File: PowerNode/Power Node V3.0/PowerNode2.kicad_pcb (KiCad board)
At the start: 2 copper layers, 78.4 x 64.8 mm, 60 parts, among them IC1 CD4511B, IC4 ACS712xLCTR-30A, IC5 74HC595N, IC7 CD4511B

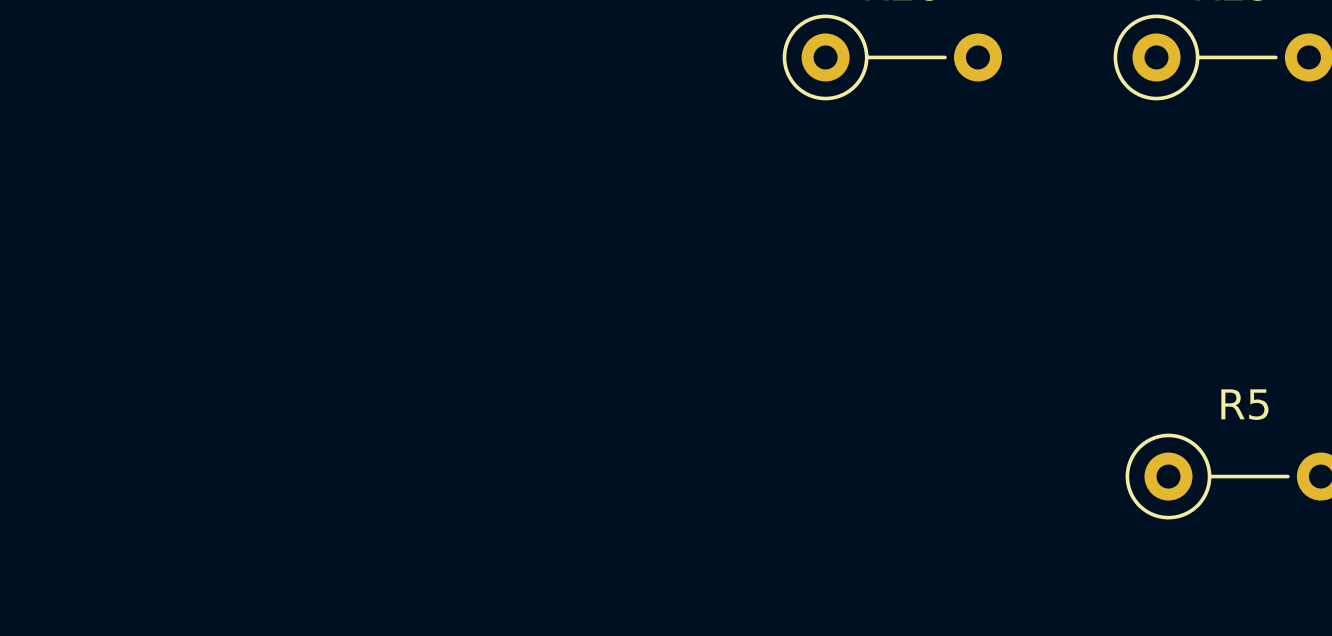
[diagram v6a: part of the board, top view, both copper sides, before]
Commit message: PN3: added logic schematic (oops) and protective diode/capacitors for ATTiny inputs
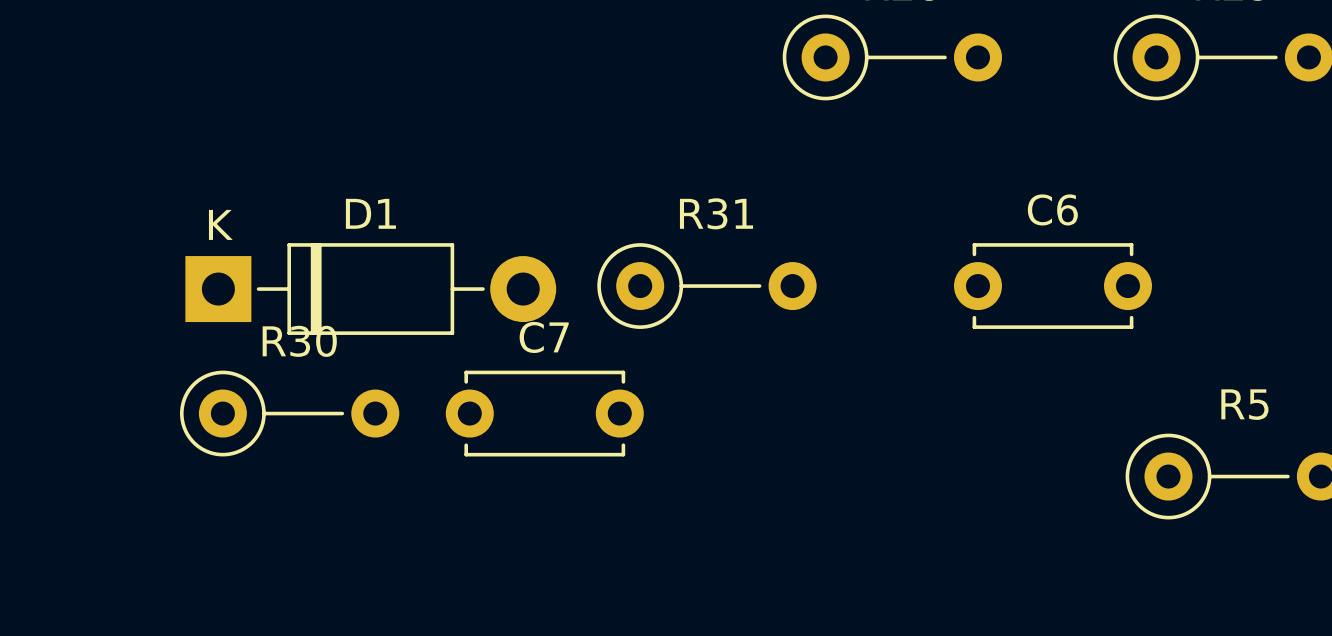
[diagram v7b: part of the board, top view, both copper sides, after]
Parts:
- added C6: 0.1uF, Capacitor_THT:C_Disc_D5.0mm_W2.5mm_P5.00mm, F.Cu at (141.0, 58.4)
- added C7: 0.1uF, Capacitor_THT:C_Disc_D5.0mm_W2.5mm_P5.00mm, F.Cu at (124.0, 62.7)
- added D1: 1N4733A, Diode_THT:D_DO-41_SOD81_P10.16mm_Horizontal, F.Cu at (115.7, 58.5)
- added R30: 110, Resistor_THT:R_Axial_DIN0207_L6.3mm_D2.5mm_P5.08mm_Vertical, F.Cu at (115.8, 62.7)
- added R31: 10k, Resistor_THT:R_Axial_DIN0207_L6.3mm_D2.5mm_P5.08mm_Vertical, F.Cu at (129.7, 58.4)
- R1: value 300k -> 10k
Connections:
- IC4 pad 7: /IMEAS -> Net-(IC4-Pad7)
- R1 pad 1: GND -> Net-(IC4-Pad7)
- R1 pad 2: /VMEAS -> /IMEAS
- U$1 pad 3: /SWITCH -> Net-(C7-Pad1)
- U$1 pad 6: /VMEAS -> Net-(D1-Pad1)

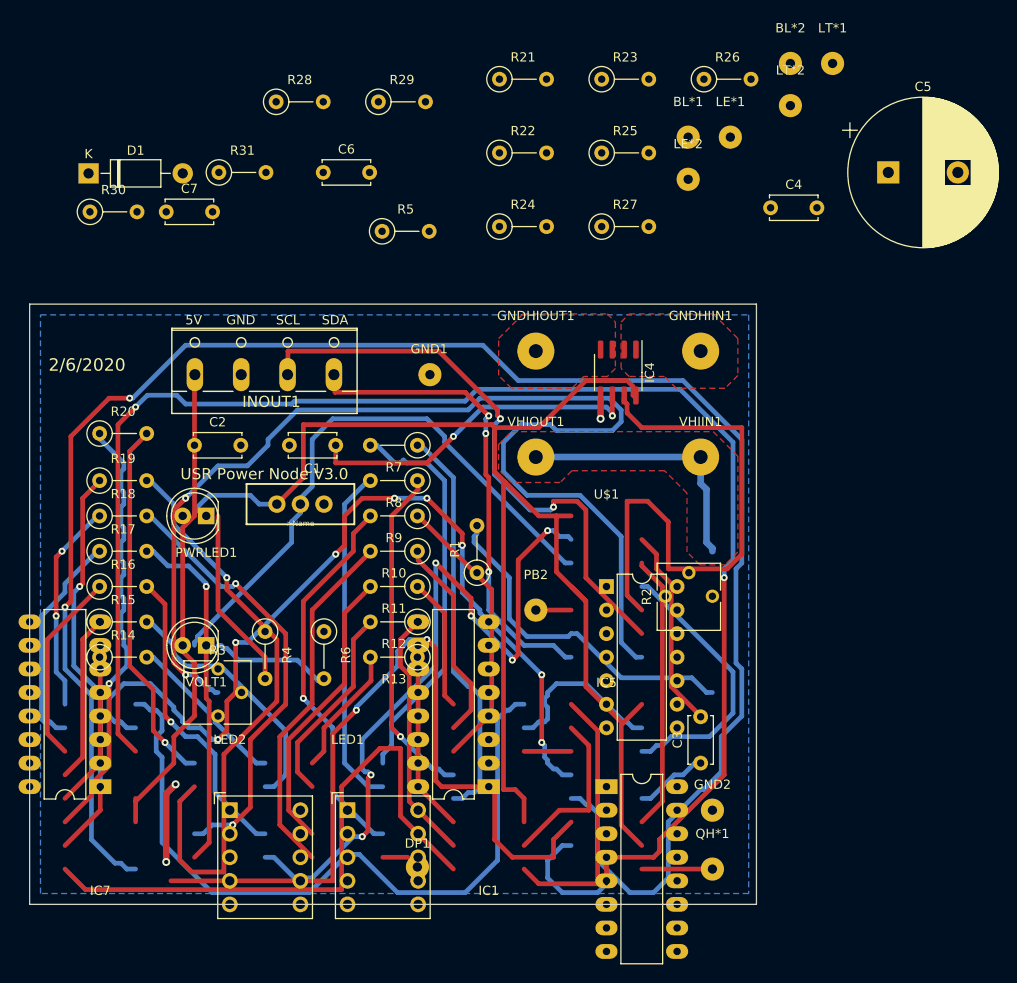
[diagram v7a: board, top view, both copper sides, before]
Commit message: PN3: removed 100uF capacitor and cleaned up some things
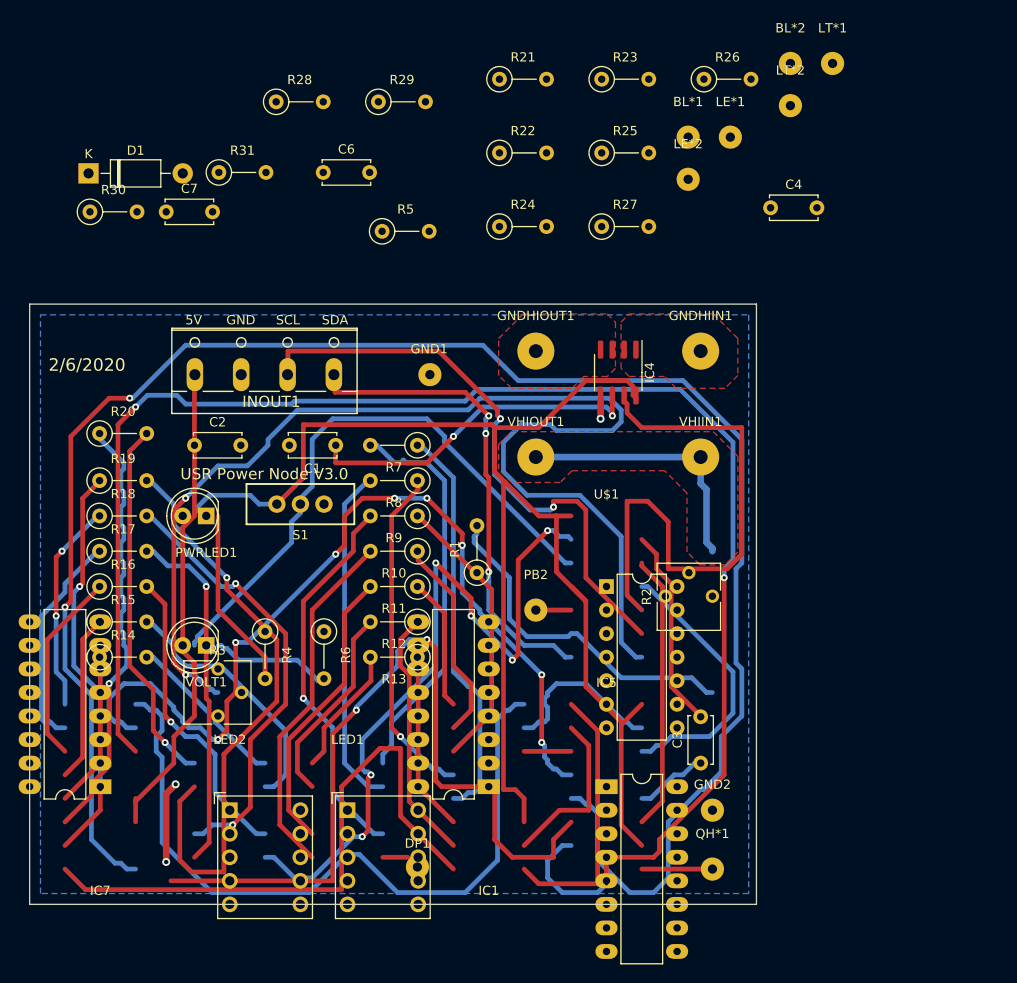
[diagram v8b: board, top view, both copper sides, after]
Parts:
- removed C5: 100uF, Capacitor_THT:CP_Radial_D16.0mm_P7.50mm
